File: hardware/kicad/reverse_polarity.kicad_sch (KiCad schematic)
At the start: 14 parts, among them J1 12V_IN, J2 12V_IN, Q1 IRF4905

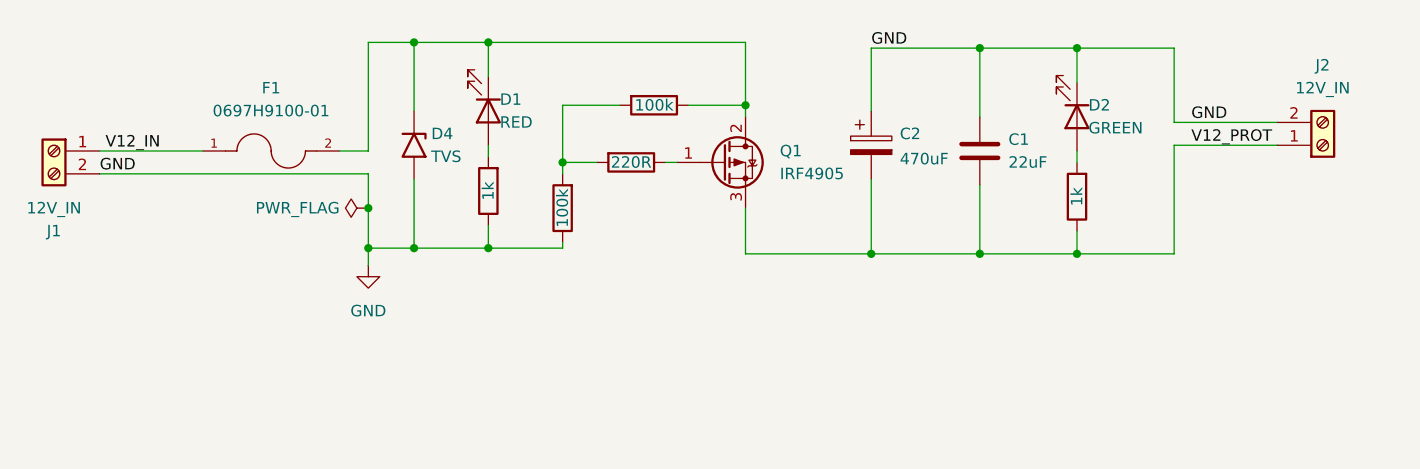
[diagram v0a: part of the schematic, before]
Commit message: feat: added reverse polarity protection pcb
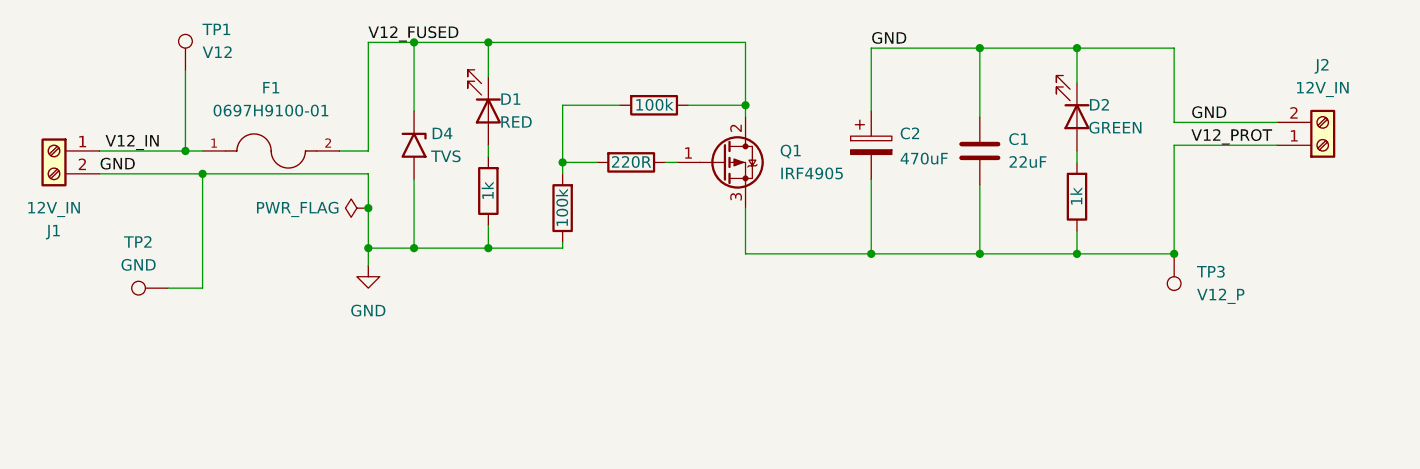
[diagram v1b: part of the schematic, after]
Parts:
- added TP1: V12, TestPoint:TestPoint_Pad_D2.5mm, symbol Connector:TestPoint
- added TP2: GND, TestPoint:TestPoint_Pad_D2.5mm, symbol Connector:TestPoint
- added TP3: V12_P, TestPoint:TestPoint_Pad_D2.5mm, symbol Connector:TestPoint
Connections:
- net GND: now also TP2.1
- net V12_IN: now also TP1.1
- net V12_PROT: now also TP3.1
- net V12_FUSED: now reaches D1.1 (K), D4.1 (A1), F1.2, Q1.2 (D), R3.1
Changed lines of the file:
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@@
 (kicad_sch (version 20230121) (generator eeschema)
   (paper "A4")
+  (junction (at 171.45 96.52) (diameter 0) (color 0 0 0 0)
+  )
   (junction (at 137.795 96.52) (diameter 0) (color 0 0 0 0)
   )
@@
   (junction (at 86.995 73.025) (diameter 0) (color 0 0 0 0)
   )
+  (junction (at 63.5 87.63) (diameter 0) (color 0 0 0 0)
+  )
   (junction (at 81.915 95.885) (diameter 0) (color 0 0 0 0)
   )
@@
   (junction (at 160.655 73.66) (diameter 0) (color 0 0 0 0)
   )
+  (junction (at 61.595 85.09) (diameter 0) (color 0 0 0 0)
+  )
   (wire (pts (xy 95.25 76.835) (xy 95.25 73.025))
     (stroke (width 0) (type default))
@@
     (stroke (width 0) (type default))
   )
+  (wire (pts (xy 61.595 85.09) (xy 63.5 85.09))
+    (stroke (width 0) (type default))
+  )
   (wire (pts (xy 171.45 84.455) (xy 182.88 84.455))
     (stroke (width 0) (type default))
@@
     (stroke (width 0) (type default))
   )
+  (wire (pts (xy 61.595 76.2) (xy 61.595 85.09))
+    (stroke (width 0) (type default))
+  )
   (wire (pts (xy 103.505 95.25) (xy 103.505 95.885))
     (stroke (width 0) (type default))
@@
     (stroke (width 0) (type default))
   )
+  (wire (pts (xy 59.69 100.33) (xy 63.5 100.33))
+    (stroke (width 0) (type default))
+  )
+  (wire (pts (xy 63.5 100.33) (xy 63.5 87.63))
+    (stroke (width 0) (type default))
+  )
   (wire (pts (xy 81.915 73.025) (xy 86.995 73.025))
     (stroke (width 0) (type default))
@@
     (stroke (width 0) (type default))
   )
-  (wire (pts (xy 52.07 87.63) (xy 81.915 87.63))
+  (wire (pts (xy 52.07 87.63) (xy 63.5 87.63))
     (stroke (width 0) (type default))
   )
@@
     (stroke (width 0) (type default))
   )
+  (wire (pts (xy 63.5 87.63) (xy 81.915 87.63))
+    (stroke (width 0) (type default))
+  )
   (wire (pts (xy 160.655 96.52) (xy 171.45 96.52))
     (stroke (width 0) (type default))
@@
     (stroke (width 0) (type default))
   )
-  (wire (pts (xy 52.07 85.09) (xy 63.5 85.09))
+  (wire (pts (xy 52.07 85.09) (xy 61.595 85.09))
     (stroke (width 0) (type default))
   )
@@
   )
   (label "V12_PROT" (at 173.355 84.455 0) (fields_autoplaced)
+    (effects (font (size 1.27 1.27)) (justify left bottom))
+  )
+  (label "V12_FUSED" (at 81.915 73.025 0) (fields_autoplaced)
     (effects (font (size 1.27 1.27)) (justify left bottom))
   )
@@
     )
   )
+  (symbol (lib_id "Connector:TestPoint") (at 61.595 76.2 0) (unit 1)
+    (in_bom yes) (on_board yes) (dnp no) (fields_autoplaced)
+    (property "Reference" "TP1" (at 63.5 71.628 0)
+      (effects (font (size 1.27 1.27)) (justify left))
+    )
+    (property "Value" "V12" (at 63.5 74.168 0)
+      (effects (font (size 1.27 1.27)) (justify left))
+    )
+    (property "Footprint" "TestPoint:TestPoint_Pad_D2.5mm" (at 66.675 76.2 0)
+      (effects (font (size 1.27 1.27)) hide)
+    )
+    (property "Datasheet" "~" (at 66.675 76.2 0)
+      (effects (font (size 1.27 1.27)) hide)
+    )
+    (pin "1")
+    (instances
+      (project "reverse_polarity"
+        (path "/9575f7c0-6ed3-4ce3-92a0-9d842220dc14"
+          (reference "TP1") (unit 1)
+        )
+      )
+    )
+  )
   (symbol (lib_id "Device:R") (at 95.25 89.535 180) (unit 1)
     (in_bom yes) (on_board yes) (dnp no)
@@
         )
       )
+    )
+  )
+  (symbol (lib_id "Connector:TestPoint") (at 59.69 100.33 90) (unit 1)
+    (in_bom yes) (on_board yes) (dnp no) (fields_autoplaced)
+    (property "Reference" "TP2" (at 56.388 95.25 90)
+      (effects (font (size 1.27 1.27)))
+    )
+    (property "Value" "GND" (at 56.388 97.79 90)
+      (effects (font (size 1.27 1.27)))
+    )
+    (property "Footprint" "TestPoint:TestPoint_Pad_D2.5mm" (at 59.69 95.25 0)
+      (effects (font (size 1.27 1.27)) hide)
+    )
+    (property "Datasheet" "~" (at 59.69 95.25 0)
+      (effects (font (size 1.27 1.27)) hide)
+    )
+    (pin "1")
+    (instances
+      (project "reverse_polarity"
+        (path "/9575f7c0-6ed3-4ce3-92a0-9d842220dc14"
+          (reference "TP2") (unit 1)
+        )
+      )
+    )
+  )
+  (symbol (lib_id "Connector:TestPoint") (at 171.45 96.52 180) (unit 1)
+    (in_bom yes) (on_board yes) (dnp no) (fields_autoplaced)
+    (property "Reference" "TP3" (at 173.99 98.552 0)
+      (effects (font (size 1.27 1.27)) (justify right))
+    )
+    (property "Value" "V12_P" (at 173.99 101.092 0)
+      (effects (font (size 1.27 1.27)) (justify right))
+    )
+    (property "Footprint" "TestPoint:TestPoint_Pad_D2.5mm" (at 166.37 96.52 0)
+      (effects (font (size 1.27 1.27)) hide)
+    )
+    (property "Datasheet" "~" (at 166.37 96.52 0)
+      (effects (font (size 1.27 1.27)) hide)
+    )
+    (pin "1")
+    (instances
+      (project "reverse_polarity"
+        (path "/9575f7c0-6ed3-4ce3-92a0-9d842220dc14"
+          (reference "TP3") (unit 1)
+        )
+      )

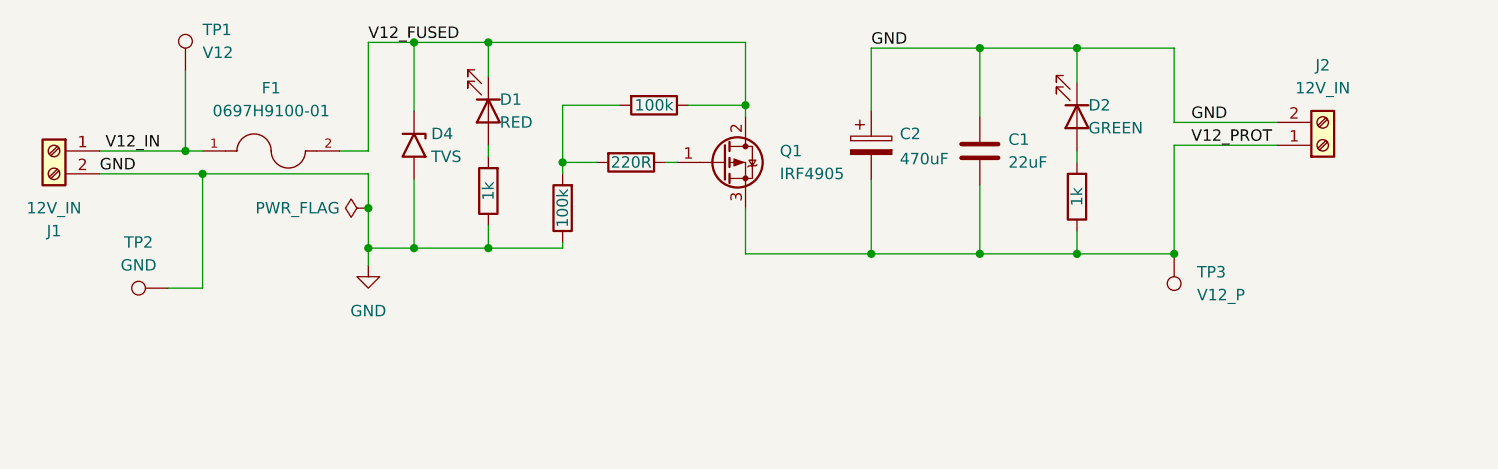
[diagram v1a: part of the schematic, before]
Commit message: fix: smd packages for reverse polarity & board orientation
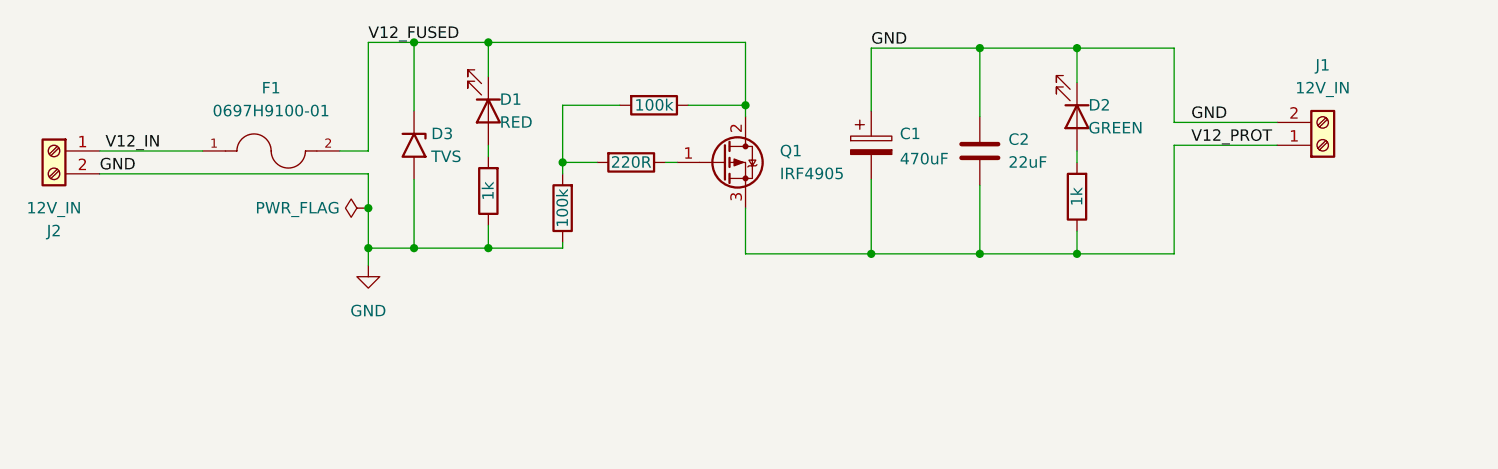
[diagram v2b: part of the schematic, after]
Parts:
- removed TP1: V12, TestPoint:TestPoint_Pad_D2.5mm, symbol Connector:TestPoint
- removed TP2: GND, TestPoint:TestPoint_Pad_D2.5mm, symbol Connector:TestPoint
- removed TP3: V12_P, TestPoint:TestPoint_Pad_D2.5mm, symbol Connector:TestPoint
- C2: renamed from C1; footprint Capacitor_THT:C_Rect_L7.0mm_W3.5mm_P5.00mm -> Capacitor_SMD:C_0805_2012Metric_Pad1.18x1.45mm_HandSolder
- R1: renamed from R3; footprint Resistor_THT:R_Axial_DIN0207_L6.3mm_D2.5mm_P10.16mm_Horizontal -> Resistor_SMD:R_0805_2012Metric_Pad1.20x1.40mm_HandSolder
- R2: footprint Resistor_THT:R_Axial_DIN0207_L6.3mm_D2.5mm_P10.16mm_Horizontal -> Resistor_SMD:R_0805_2012Metric_Pad1.20x1.40mm_HandSolder
- R5: renamed from R4; footprint Resistor_THT:R_Axial_DIN0207_L6.3mm_D2.5mm_P10.16mm_Horizontal -> Resistor_SMD:R_0805_2012Metric_Pad1.20x1.40mm_HandSolder
- renumbered C2 to C1, D4 to D3, J2 to J1, J1 to J2, R1 to R3, R5 to R4

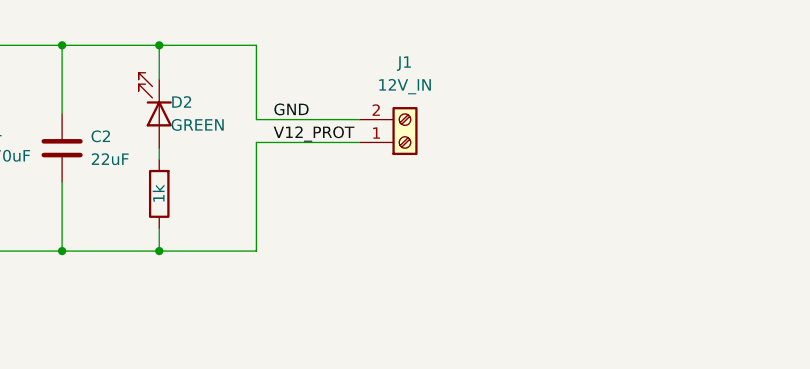
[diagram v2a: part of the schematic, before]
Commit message: docs: added bom, 3d & prints(pcb) - reverse polarity
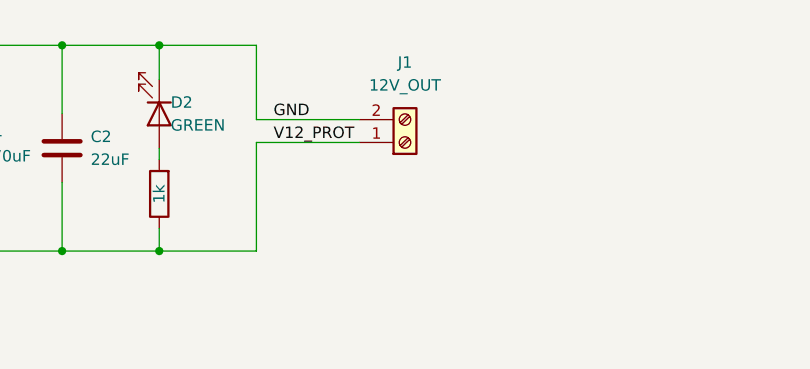
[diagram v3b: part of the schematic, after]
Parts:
- J1: value 12V_IN -> 12V_OUT
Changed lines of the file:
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@@
       (effects (font (size 1.27 1.27)))
     )
-    (property "Value" "12V_IN" (at 187.96 78.105 0)
+    (property "Value" "12V_OUT" (at 187.96 78.105 0)
       (effects (font (size 1.27 1.27)))
     )
